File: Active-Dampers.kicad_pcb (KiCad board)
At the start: 2 copper layers, 65 x 50 mm, 62 parts, among them J1 PINHD_1x2_Male, J2 Conn_01x04, J3 Conn_01x04, J4 Conn_01x02, J5 Conn_01x04, J6 USB_C_Receptacle_USB2.0_16P, J7 Conn_01x04, J8 Barrel_Jack_Switch_Pin3Ring, SW2 SW_SPST, U1 TPS5430DDAR, U10 L80-R, U2 DRV8848, U3 ESP32-S3-MINI-1, U4 DRV8848, U5 DRV8848, U6 AMS1117-3.3, U7 DRV8848, U8 SN65HVD230

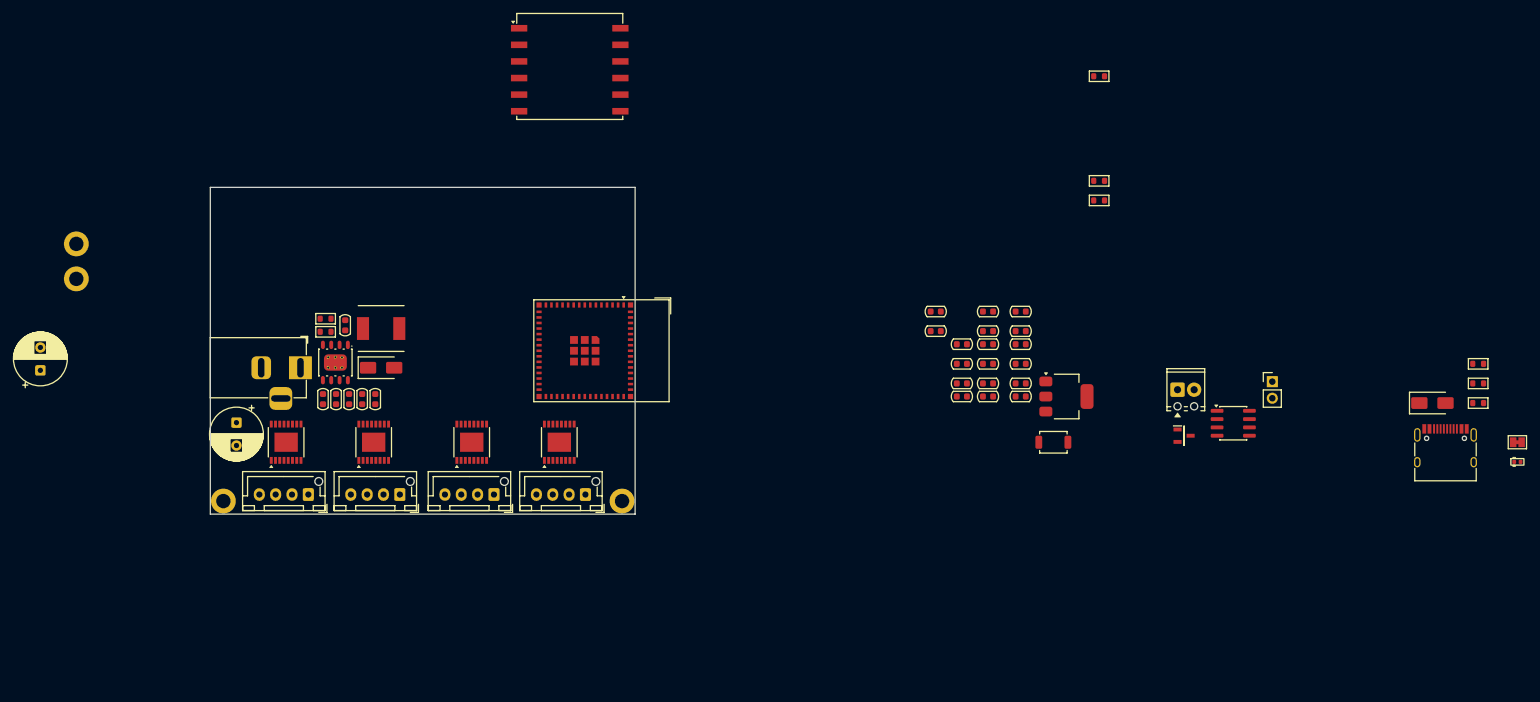
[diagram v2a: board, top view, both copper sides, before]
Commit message: add cubemx project and redo some layour with new parts
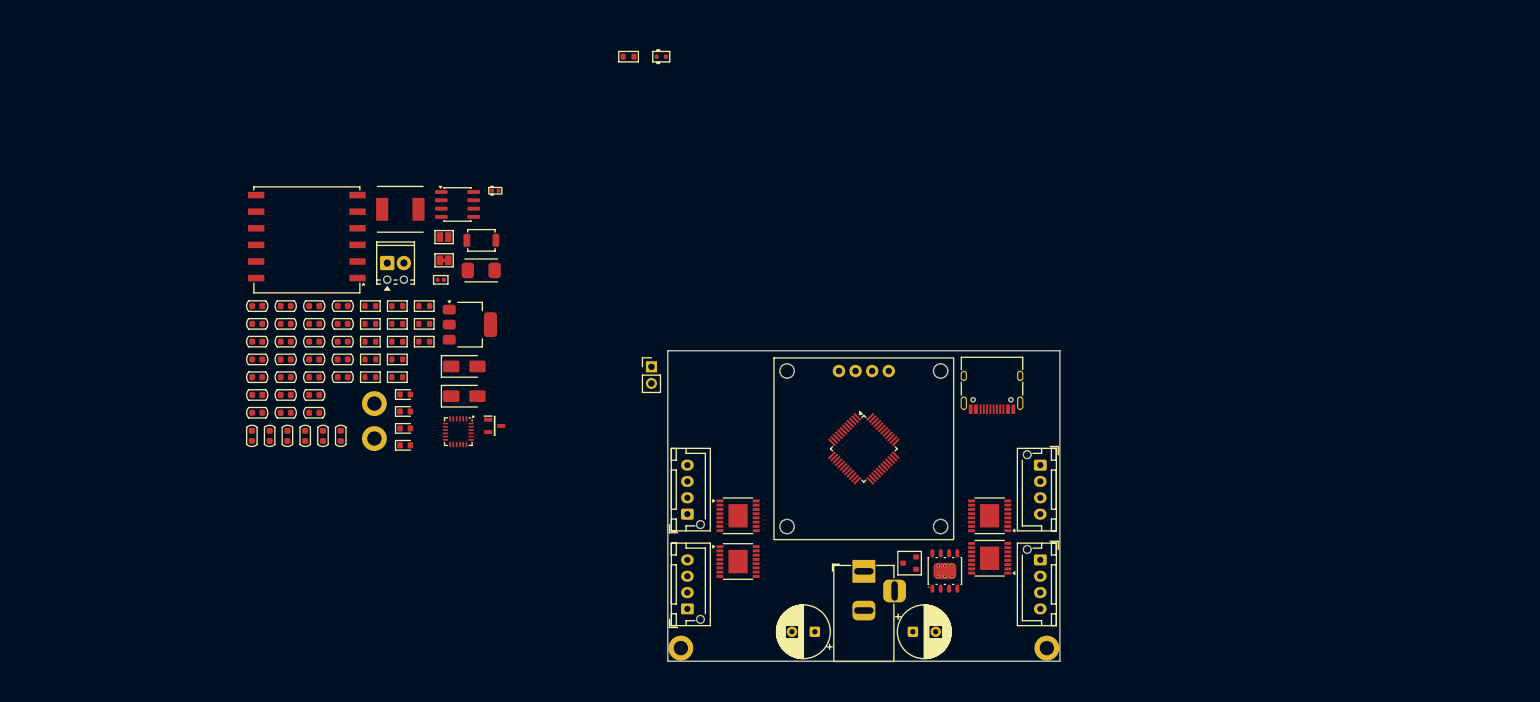
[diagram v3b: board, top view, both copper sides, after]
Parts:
- removed D8: LED BLUE, PCM_LED_SMD_AKL:LED_0402_1005Metric
- removed D9: SS54, PCM_JLCPCB:D_SMA
- removed R11: 3.24k, PCM_Resistor_SMD_AKL:R_0603_1608Metric
- removed R16: 120, PCM_Resistor_SMD_AKL:R_0603_1608Metric
- removed R23: 1k, PCM_Resistor_SMD_AKL:R_0603_1608Metric
- removed SW2: SW_SPST, Button_Switch_SMD:SW_SPST_TS-1088-xR025
- removed U3: ESP32-S3-MINI-1, RF_Module:ESP32-S2-MINI-1
- removed U5: DRV8848, Package_SO:TSSOP-16-1EP_4.4x5mm_P0.65mm
- added C25: 22uF, PCM_Capacitor_SMD_AKL:C_0603_1608Metric, F.Cu at (65.9, 73.6)
- added C26: 100nF, PCM_Capacitor_SMD_AKL:C_0603_1608Metric, F.Cu at (65.9, 76.3)
- added C27: 22uF, PCM_Capacitor_SMD_AKL:C_0603_1608Metric, F.Cu at (65.9, 79.0)
- added C28: 22uF, PCM_Capacitor_SMD_AKL:C_0603_1608Metric, F.Cu at (65.9, 81.8)
- added C29: 22uF, PCM_Capacitor_SMD_AKL:C_0603_1608Metric, F.Cu at (65.9, 84.5)
- added C30: 22uF, PCM_Capacitor_SMD_AKL:C_0603_1608Metric, F.Cu at (70.3, 68.2)
- added C31: 0.1uF, PCM_Capacitor_SMD_AKL:C_0603_1608Metric, F.Cu at (70.3, 70.9)
- added C34: 0.1uF, PCM_Capacitor_SMD_AKL:C_0603_1608Metric, F.Cu at (70.3, 79.0)
- added D1: SS54, PCM_JLCPCB:D_SMA, F.Cu at (88.9, 77.4)
- added D12: LED BLUE, LED_SMD:LED_0603_1608Metric, F.Cu at (79.8, 84.3)
- added D14: LED BLUE, LED_SMD:LED_0603_1608Metric, F.Cu at (79.8, 86.9)
- added D19: LED BLUE, LED_SMD:LED_0603_1608Metric, F.Cu at (79.8, 89.5)
- added D4: CDSOT23-T24CAN, SamacSys_Parts:SOT95P230X117-3N, F.Cu at (93.5, 86.5)
- added D7: LED BLUE, LED_SMD:LED_0603_1608Metric, F.Cu at (79.8, 81.7)
- added DZ1: BZT52C18T, PCM_Diode_SMD_AKL:D_SOD-523, F.Cu at (119.0, 30.0)
- added FB1: MMZ1005F181ETD25, PCM_Ferrite_SMD_AKL:Ferrite_0402_1005Metric, F.Cu at (85.3, 64.1)
- added J9: PINHD_1x2_Male, Connector_PinHeader_2.54mm:PinHeader_1x02_P2.54mm_Vertical, F.Cu at (117.5, 77.5)
- added JP2: SolderJumper_2_Bridged, Jumper:SolderJumper-2_P1.3mm_Bridged_Pad1.0x1.5mm, F.Cu at (85.8, 61.2)
- added Q1: AO3401A, PCM_Package_TO_SOT_SMD_AKL:SOT-23, F.Cu at (157.0, 107.5)
- added R13: 330, PCM_Resistor_SMD_AKL:R_0603_1608Metric, F.Cu at (78.6, 79.0)
- added R2: 10k, PCM_Resistor_SMD_AKL:R_0603_1608Metric, F.Cu at (74.5, 70.9)
- added R28: 680, PCM_Resistor_SMD_AKL:R_0603_1608Metric, F.Cu at (82.7, 68.2)
- added R3: 5k1, PCM_Resistor_SMD_AKL:R_0603_1608Metric, F.Cu at (74.5, 73.6)
- added R30: 2k, PCM_Resistor_SMD_AKL:R_0603_1608Metric, F.Cu at (82.7, 70.9)
- added R36: 2k, PCM_Resistor_SMD_AKL:R_0603_1608Metric, F.Cu at (82.7, 73.6)
- added R4: 5k1, PCM_Resistor_SMD_AKL:R_0603_1608Metric, F.Cu at (74.5, 76.3)
- added R5: 10k, PCM_Resistor_SMD_AKL:R_0603_1608Metric, F.Cu at (114.0, 30.0)
- added R9: 10k, PCM_Resistor_SMD_AKL:R_0603_1608Metric, F.Cu at (78.6, 73.6)
- added SW1: SW_SPST, Button_Switch_SMD:SW_SPST_TS-1088-xR025, F.Cu at (91.5, 58.1)
- added U11: AMS1117-3.3, Package_TO_SOT_SMD:SOT-223-3_TabPin2, F.Cu at (89.7, 71.0)
- added U12: SN65HVD230, Package_SO:SOIC-8_3.9x4.9mm_P1.27mm, F.Cu at (87.8, 52.6)
- added U9: DRV8848, Package_SO:TSSOP-16-1EP_4.4x5mm_P0.65mm, F.Cu at (169.2, 106.8)
- added X1: X50328MSB2GI, PCM_JLCPCB:CRYSTAL-SMD_L5.0-W3.2, F.Cu at (91.5, 62.7)
- C1: value 1uF -> 100nF
- C10: value 220uF -> 2.2nF; footprint Capacitor_THT:CP_Radial_D8.0mm_P3.50mm -> PCM_Capacitor_SMD_AKL:C_0603_1608Metric
- C11, C12, C13: value 22uF -> 2.2uF
- C14: value 100nF -> 2.2uF
- C15: value 22uF -> 220uF; footprint PCM_Capacitor_SMD_AKL:C_0603_1608Metric -> Capacitor_THT:CP_Radial_D8.0mm_P3.50mm
- C16, C17, C18: value 22uF -> 22nF
- C19: value 0.1uF -> 22nF
- C2: value 10uF -> 22pF
- C20: value 2.2uF -> 22nF
- C21: value 2.2uF -> 10nF
- C22: value 10uF -> 220uF; footprint PCM_Capacitor_SMD_AKL:C_0603_1608Metric -> Capacitor_THT:CP_Radial_D8.0mm_P3.50mm
- C23, C24: value 2.2uF -> 22uF
- C3: value 220uF -> 22pF; footprint Capacitor_THT:CP_Radial_D8.0mm_P3.50mm -> PCM_Capacitor_SMD_AKL:C_0603_1608Metric
- C4, C5, C8: value 22nF -> 10uF
- C6: value 22nF -> 100nF
- C7: value 22nF -> 1uF
- C9: value 10nF -> 10uF
- D2: value SS54 -> LED BLUE; footprint PCM_JLCPCB:D_SMA -> PCM_LED_SMD_AKL:LED_0402_1005Metric
- D3: value CDSOT23-T24CAN -> SS54; footprint SamacSys_Parts:SOT95P230X117-3N -> PCM_JLCPCB:D_SMA
- J1: value PINHD_1x2_Male -> Conn_01x02; footprint Connector_PinHeader_2.54mm:PinHeader_1x02_P2.54mm_Vertical -> TerminalBlock_Phoenix:TerminalBlock_Phoenix_MPT-0,5-2-2.54_1x02_P2.54mm_Horizontal
- J2: value Conn_01x04 -> FL
- J3: value Conn_01x04 -> FR
- J4: value Conn_01x02 -> RL; footprint TerminalBlock_Phoenix:TerminalBlock_Phoenix_MPT-0,5-2-2.54_1x02_P2.54mm_Horizontal -> Connector_JST:JST_XH_B4B-XH-AM_1x04_P2.50mm_Vertical
- J5: value Conn_01x04 -> RR
- J6: value USB_C_Receptacle_USB2.0_16P -> Barrel_Jack_Switch_Pin3Ring; footprint Connector_USB:USB_C_Receptacle_HRO_TYPE-C-31-M-12 -> Connector_BarrelJack:BarrelJack_Horizontal
- J7: value Conn_01x04 -> USB_C_Receptacle_USB2.0_16P; footprint Connector_JST:JST_XH_B4B-XH-AM_1x04_P2.50mm_Vertical -> Connector_USB:USB_C_Receptacle_HRO_TYPE-C-31-M-12
- J8: value Barrel_Jack_Switch_Pin3Ring -> OLED; footprint Connector_BarrelJack:BarrelJack_Horizontal -> PCM_SparkFun-Display:OLED_0.96
- JP1: value SolderJumper_2_Bridged -> SolderJumper_2_Open; footprint Jumper:SolderJumper-2_P1.3mm_Bridged_Pad1.0x1.5mm -> Jumper:SolderJumper-2_P1.3mm_Open_Pad1.0x1.5mm
- R1: value 10k -> 1k
- R10: value 10k -> 120
- R6: value 5k1 -> 2k2
- R7: value 5k1 -> 10k
- R8: value 2k2 -> 3.24k
- U1: value TPS5430DDAR -> MPU-6050; footprint PCM_JLCPCB:ESOP-8_L4.9-W3.9-P1.27-LS6.0-TL-EP -> PCM_SparkFun-Semiconductor-Standard:QFN-24-1EP_4x4mm_P0.5mm
- U10: value L80-R -> TPS5430DDAR; footprint RF_GPS:Quectel_L80-R -> PCM_JLCPCB:ESOP-8_L4.9-W3.9-P1.27-LS6.0-TL-EP
- U2: value DRV8848 -> STM32F103C8T6; footprint Package_SO:TSSOP-16-1EP_4.4x5mm_P0.65mm -> PCM_JLCPCB:LQFP-48_7x7mm_P0.5mm
- U4: value DRV8848 -> L80-R; footprint Package_SO:TSSOP-16-1EP_4.4x5mm_P0.65mm -> RF_GPS:Quectel_L80-R
- U6: value AMS1117-3.3 -> DRV8848; footprint Package_TO_SOT_SMD:SOT-223-3_TabPin2 -> Package_SO:TSSOP-16-1EP_4.4x5mm_P0.65mm
- U8: value SN65HVD230 -> DRV8848; footprint Package_SO:SOIC-8_3.9x4.9mm_P1.27mm -> Package_SO:TSSOP-16-1EP_4.4x5mm_P0.65mm
- moved R6 169.5 mm to (74.5, 79.0)
- moved JP1 167.2 mm to (85.8, 57.6)
- moved R8 165.8 mm to (78.6, 70.9)
- moved R7 165.8 mm to (78.6, 68.2)
- moved H3 160.9 mm to (178.0, 120.5)
- moved J1 136.6 mm to (77.1, 61.6)
- moved R1 116.9 mm to (74.5, 68.2)
- moved C21 113.5 mm to (61.5, 84.5)
- moved D3 110.3 mm to (88.9, 82.0)
- moved H4 108.4 mm to (122.0, 120.5)
- moved C24 108.3 mm to (65.9, 70.9)
- moved C23 108.3 mm to (65.9, 68.2)
- moved C11 107.9 mm to (57.2, 79.0)
- moved C12 107.9 mm to (57.2, 81.8)
- moved C13 107.9 mm to (57.2, 84.5)
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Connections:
- C1 pad 2: +3.3V -> Net-(SW1-A)
- C10 pad 1: +5V -> Net-(U1-CPOUT)
- C11 pad 2: +5V -> Net-(U7-VINT)
- C12 pad 2: +5V -> Net-(U8-VINT)
- C13 pad 2: +5V -> Net-(U9-VINT)
- C14 pad 2: +5V -> Net-(U6-VINT)
- C15 pad 1: GND -> +12V
- C15 pad 2: +5V -> GND
- C16 pad 2: +3.3V -> +12V
- C17 pad 2: +3.3V -> +12V
- C18 pad 2: +3.3V -> +12V
- C19 pad 1: +3.3V -> GND
- C19 pad 2: GND -> +12V
- C2 pad 2: +3.3V -> Net-(U2-PD0)
- C20 pad 2: Net-(U2-VINT) -> +12V
- C21 pad 1: GND -> Net-(U10-BOOT)
- C21 pad 2: Net-(U4-VINT) -> Net-(U10-PH)
- C22 pad 1: Net-(SW2-A) -> +5V
- C23 pad 2: Net-(U5-VINT) -> +5V
- C24 pad 2: Net-(U7-VINT) -> +5V
- C3 pad 1: +12V -> GND
- C3 pad 2: GND -> Net-(U2-PD1)
- C4 pad 2: +12V -> +3.3V
- C5 pad 2: +12V -> +3.3V
- C6 pad 2: +12V -> +3.3V
- C7 pad 2: +12V -> +3.3V
- C8 pad 2: +12V -> +3.3V
- C9 pad 1: Net-(U1-BOOT) -> GND
- C9 pad 2: Net-(U1-PH) -> +3.3V
- D2 pad 1: Net-(U1-PH) -> GND
- D2 pad 2: GND -> Net-(D2-A)
- D3 pad 1: /CAN/CAN_H -> Net-(U10-PH)
- D3 pad 2: /CAN/CAN_L -> GND
- J1 pad 1: Net-(J1-Pad1) -> /CAN/CAN_L
- J1 pad 2: /CAN/CAN_L -> /CAN/CAN_H
- J2 pad 1: /BOUT_1_2 -> /BOUT1_FL
- J2 pad 2: /BOUT_1_1 -> /BOUT1_FL
- J2 pad 3: /AOUT_1_2 -> /AOUT1_FL
- J2 pad 4: /AOUT_1_1 -> /AOUT1_FL
- J3 pad 1: /BOUT_2_2 -> /BOUT2_FR
- J3 pad 2: /BOUT_1_2 -> /BOUT1_FR
- J3 pad 3: /AOUT_2_2 -> /AOUT2_FR
- J3 pad 4: /AOUT_1_2 -> /AOUT1_FR
- J4 pad 1: /CAN/CAN_L -> /BOUT2_RL
- J4 pad 2: /CAN/CAN_H -> /BOUT1_RL
- J5 pad 1: /BOUT_2_3 -> /BOUT2_RR
- J5 pad 2: /BOUT_1_3 -> /BOUT1_RR
- J5 pad 3: /AOUT_2_3 -> /AOUT2_RR
- J5 pad 4: /AOUT_1_3 -> /AOUT1_RR
- J8 pad 1: +12V -> GND
- J8 pad 2: GND -> +3.3V
- J8 pad 3: GND -> /SDA
- JP1 pad 1: Net-(JP1-A) -> VIN
- JP1 pad 2: +5V -> +12V
- L1 pad 1: Net-(U1-PH) -> Net-(U10-PH)
- R1 pad 1: GND -> +3.3V
- R1 pad 2: Net-(U8-Rs) -> Net-(SW1-A)
- R10 pad 1: Net-(U1-VSENSE) -> Net-(J9-Pad1)
- R10 pad 2: +5V -> /CAN/CAN_H
- R6 pad 1: Net-(J6-CC1) -> Net-(D1-Pad2)
- R6 pad 2: GND -> Net-(D2-A)
- R7 pad 1: Net-(J6-CC2) -> Net-(U10-VSENSE)
- R7 pad 2: GND -> +5V
- R8 pad 1: Net-(D9-Pad2) -> GND
- R8 pad 2: Net-(D8-A) -> Net-(U10-VSENSE)
- U1 pad 1: Net-(U1-BOOT) -> unconnected-(U1-CLKIN-Pad1)
- U1 pad 4: Net-(U1-VSENSE) -> unconnected-(U1-NC-Pad4)
- U1 pad 6: GND -> unconnected-(U1-AUX_DA-Pad6)
- U1 pad 7: +12V -> unconnected-(U1-AUX_CL-Pad7)
- U1 pad 8: Net-(U1-PH) -> +3.3V
- U1 pad 9: GND -> unconnected-(U1-AD0-Pad9)
- U10 pad 1: /GPS_RX -> Net-(U10-BOOT)
- U10 pad 2: /GPS_TX -> unconnected-(U10-NC-Pad2)
- U10 pad 3: GND -> unconnected-(U10-NC-Pad3)
- U10 pad 4: +3.3V -> Net-(U10-VSENSE)
- U10 pad 5: +3.3V -> unconnected-(U10-ENA-Pad5)
- U10 pad 6: unconnected-(U10-1PPS-Pad6) -> GND
- U10 pad 7: unconnected-(U10-RESERVED-Pad7) -> +12V
- U10 pad 8: unconnected-(U10-RESERVED-Pad8) -> Net-(U10-PH)
- U10 pad 9: unconnected-(U10-NC-Pad9) -> GND
- U2 pad 1: /~{SLEEP}_1 -> +3.3V
- U2 pad 10: /BIN2_1 -> /AIN1_FL
- U2 pad 11: +3.3V -> /BIN1_FL
- U2 pad 12: +12V -> /AIN1_FR
- U2 pad 13: GND -> /BIN1_FR
- U2 pad 14: Net-(U2-VINT) -> /AIN2_FL
- U2 pad 15: /AIN2_1 -> /BIN2_FL
- U2 pad 16: /AIN1_1 -> /AIN1_RL
- U2 pad 17: GND -> /BIN1_RL
- U2 pad 2: /AOUT_1_1 -> unconnected-(U2-PC13-Pad2)
- U2 pad 4: /AOUT_1_2 -> unconnected-(U2-PC15-Pad4)
- U2 pad 5: /BOUT_1_2 -> Net-(U2-PD0)
- U2 pad 6: unconnected-(U2-BISEN-Pad6) -> Net-(U2-PD1)
- U2 pad 7: /BOUT_1_1 -> Net-(SW1-A)
- U2 pad 8: /~{FAULT}_1 -> GND
- U2 pad 9: /BIN1_1 -> Net-(U2-VDDA)
- U4 pad 1: /~{SLEEP}_2 -> /GPS_RX
- U4 pad 10: /BIN2_2 -> unconnected-(U4-~{RESET}-Pad10)
- U4 pad 11: +3.3V -> unconnected-(U4-RESERVED-Pad11)
- U4 pad 12: +12V -> GND
- U4 pad 2: /AOUT_1_2 -> /GPS_TX
- U4 pad 3: unconnected-(U4-AISEN-Pad3) -> GND
- U4 pad 4: /AOUT_2_2 -> +3.3V
- U4 pad 5: /BOUT_2_2 -> +3.3V
- U4 pad 7: /BOUT_1_2 -> unconnected-(U4-RESERVED-Pad7)
- U4 pad 8: /~{FAULT}_2 -> unconnected-(U4-RESERVED-Pad8)
- U4 pad 9: /BIN1_2 -> unconnected-(U4-NC-Pad9)
- U6 pad 1: GND -> /~{SLEEP}
- U6 pad 2: +3.3V -> /AOUT1_FL
- U6 pad 3: +5V -> unconnected-(U6-AISEN-Pad3)
- U7 pad 1: /~{SLEEP}_4 -> /~{SLEEP}
- U7 pad 10: /BIN2_4 -> /BIN2_FR
- U7 pad 15: /AIN2_4 -> /AIN2_FR
- U7 pad 16: /AIN1_4 -> /AIN1_FR
- U7 pad 2: /AOUT_1_3 -> /AOUT1_FR
- U7 pad 4: /AOUT_2_3 -> /AOUT2_FR
- U7 pad 5: /BOUT_2_3 -> /BOUT2_FR
- U7 pad 7: /BOUT_1_3 -> /BOUT1_FR
- U7 pad 8: /~{FAULT}_4 -> /~{FAULT}_FR
- U7 pad 9: /BIN1_4 -> /BIN1_FR
- U8 pad 1: /CAN_TX -> /~{SLEEP}
- U8 pad 2: GND -> /AOUT1_RL
- U8 pad 3: +3.3V -> unconnected-(U8-AISEN-Pad3)
- U8 pad 4: /CAN_RX -> /AOUT2_RL
- U8 pad 5: unconnected-(U8-Vref-Pad5) -> /BOUT2_RL
- U8 pad 6: /CAN/CAN_L -> unconnected-(U8-BISEN-Pad6)
- U8 pad 7: /CAN/CAN_H -> /BOUT1_RL
- U8 pad 8: Net-(U8-Rs) -> /~{FAULT}_RL
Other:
- board size 65 x 50 mm -> 60 x 47.5 mm
- copper layers 2 -> 4

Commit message: keep working on pcb
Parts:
- removed C31: 0.1uF, PCM_Capacitor_SMD_AKL:C_0603_1608Metric
- removed C32, C33: 100pF, PCM_Capacitor_SMD_AKL:C_0603_1608Metric
- removed C4: 10uF, PCM_Capacitor_SMD_AKL:C_0603_1608Metric
- removed D19: LED BLUE, LED_SMD:LED_0603_1608Metric
- removed D2: LED BLUE, PCM_LED_SMD_AKL:LED_0402_1005Metric
- removed D4: CDSOT23-T24CAN, SamacSys_Parts:SOT95P230X117-3N
- removed DZ1: BZT52C18T, PCM_Diode_SMD_AKL:D_SOD-523
- removed FB1: MMZ1005F181ETD25, PCM_Ferrite_SMD_AKL:Ferrite_0402_1005Metric
- removed H1: MountingHole_M3_3.2mm_Pad, MountingHole:MountingHole_2.2mm_M2_ISO14580_Pad
- removed J9: PINHD_1x2_Male, Connector_PinHeader_2.54mm:PinHeader_1x02_P2.54mm_Vertical
- removed JP1: SolderJumper_2_Open, Jumper:SolderJumper-2_P1.3mm_Open_Pad1.0x1.5mm
- removed Q1: AO3401A, PCM_Package_TO_SOT_SMD_AKL:SOT-23
- removed R10: 120, PCM_Resistor_SMD_AKL:R_0603_1608Metric
- removed R36: 2k, PCM_Resistor_SMD_AKL:R_0603_1608Metric
- removed R6: 2k2, PCM_Resistor_SMD_AKL:R_0603_1608Metric
- removed R9: 10k, PCM_Resistor_SMD_AKL:R_0603_1608Metric
- removed U12: SN65HVD230, Package_SO:SOIC-8_3.9x4.9mm_P1.27mm
- removed U4: L80-R, RF_GPS:Quectel_L80-R
- added R16: 4.7k, PCM_Resistor_SMD_AKL:R_0402_1005Metric, F.Cu at (119.9, 90.0)
- J1: value Conn_01x02 -> Conn_ARM_JTAG_SWD_10; footprint TerminalBlock_Phoenix:TerminalBlock_Phoenix_MPT-0,5-2-2.54_1x02_P2.54mm_Horizontal -> Manual_Parts:CNC_3220-10-0300-00
- R5: value 10k -> 4.7k; footprint PCM_Resistor_SMD_AKL:R_0603_1608Metric -> PCM_Resistor_SMD_AKL:R_0402_1005Metric
- moved C13 106.6 mm to (161.5, 106.2), turned to 180 degrees
- moved C11 102.4 mm to (158.0, 96.8)
- moved C23 99.3 mm to (156.7, 108.2)
- moved C24 98.9 mm to (156.7, 110.0)
- moved C25 98.5 mm to (156.7, 111.8)
- moved H2 98.2 mm to (172.8, 78.2)
- moved R3 94.7 mm to (169.0, 79.8), turned to 90 degrees
- moved C30 94.6 mm to (156.7, 106.5), turned to 180 degrees
- moved C28 93.7 mm to (156.7, 104.8), turned to 180 degrees
- moved C29 92.7 mm to (156.7, 103.0), turned to 180 degrees
- moved R4 92.3 mm to (166.8, 79.8), turned to 90 degrees
- moved C6 91.0 mm to (155.5, 89.5), turned to 180 degrees
- moved C16 89.6 mm to (142.5, 109.2)
- moved C17 89.2 mm to (142.5, 111.0)
- moved C18 88.7 mm to (142.5, 112.5)
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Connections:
- C1 pad 2: Net-(SW1-A) -> Net-(J1-~{RESET})
- J1 pad 1: /CAN/CAN_L -> +3.3V
- J1 pad 2: /CAN/CAN_H -> /SWDIO/TMS
- J2 pad 1: /BOUT1_FL -> /BOUT2_FL
- J2 pad 3: /AOUT1_FL -> /AOUT2_FL
- J6 pad 1: VIN -> +12V
- R1 pad 2: Net-(SW1-A) -> Net-(J1-~{RESET})
- R5 pad 1: GND -> +3.3V
- R5 pad 2: Net-(DZ1-A) -> /SCL
- SW1 pad 1: Net-(SW1-A) -> Net-(J1-~{RESET})
- U2 pad 2: unconnected-(U2-PC13-Pad2) -> /~{FAULT}_FL
- U2 pad 28: unconnected-(U2-PB15-Pad28) -> /~{FAULT}_RR
- U2 pad 29: unconnected-(U2-PA8-Pad29) -> /~{FAULT}_FR
- U2 pad 3: unconnected-(U2-PC14-Pad3) -> /~{FAULT}_RL
- U2 pad 34: /AIN2_FR -> /SWDIO/TMS
- U2 pad 37: /BIN2_FR -> /SWCLK/TCK
- U2 pad 39: /~{SLEEP} -> /SWO/TDO
- U2 pad 40: /~{FAULT}_FL -> /~{SLEEP}
- U2 pad 41: /~{FAULT}_FR -> unconnected-(U2-PB5-Pad41)
- U2 pad 42: /~{FAULT}_RL -> unconnected-(U2-PB6-Pad42)
- U2 pad 43: /~{FAULT}_RR -> unconnected-(U2-PB7-Pad43)
- U2 pad 7: Net-(SW1-A) -> Net-(J1-~{RESET})
- U2 pad 9: Net-(U2-VDDA) -> +3.3V
- U6 pad 4: /AOUT1_FL -> /AOUT2_FL
- U6 pad 5: /BOUT1_FL -> /BOUT2_FL
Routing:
- net +5V: track 0.00 -> 71.9 mm, vias 0 -> 11
- net /~{SLEEP}: track 0.00 -> 57.9 mm, vias 0 -> 3
- net +3.3V: track 0.00 -> 32.3 mm, vias 0 -> 15
- net /~{FAULT}_RL: track 0.00 -> 26.9 mm, vias 0 -> 2
- net /~{FAULT}_FL: track 0.00 -> 20.6 mm, vias 0 -> 2
- net /USB-: track 0.00 -> 20.3 mm, vias 0 -> 2
- net /USB+: track 0.00 -> 20.1 mm, vias 0 -> 2
- net /BOUT2_RL: track 0.00 -> 18.7 mm, vias 0 -> 1
- net /AOUT1_RR: track 0.00 -> 16.9 mm
- net /BIN1_FR: track 0.00 -> 16.5 mm, vias 0 -> 2
- net /BOUT1_RR: track 0.00 -> 16.2 mm
- net /AIN1_FR: track 0.00 -> 16.2 mm, vias 0 -> 2
- net /BIN2_RL: track 0.00 -> 15.5 mm
- net /AOUT2_RR: track 0.00 -> 15.5 mm
- net /AIN1_RR: track 0.00 -> 15.1 mm, vias 0 -> 2
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- added copper zone on In2.Cu, net +12V
- added copper zone on B.Cu, net +3.3V
- added copper zone on B.Cu, net +5V
- added copper zone on F.Cu, net GND
- added copper zone on In1.Cu, net GND
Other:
- board size 60 x 47.5 mm -> 50 x 50 mm
- board text added: "U7"
